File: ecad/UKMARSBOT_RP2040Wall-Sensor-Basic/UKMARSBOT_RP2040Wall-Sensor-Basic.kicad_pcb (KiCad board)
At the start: 2 copper layers, 80 x 31.2 mm, 32 parts, among them J1 Conn_01x16, T1 BC337-40, T2 BC337-40

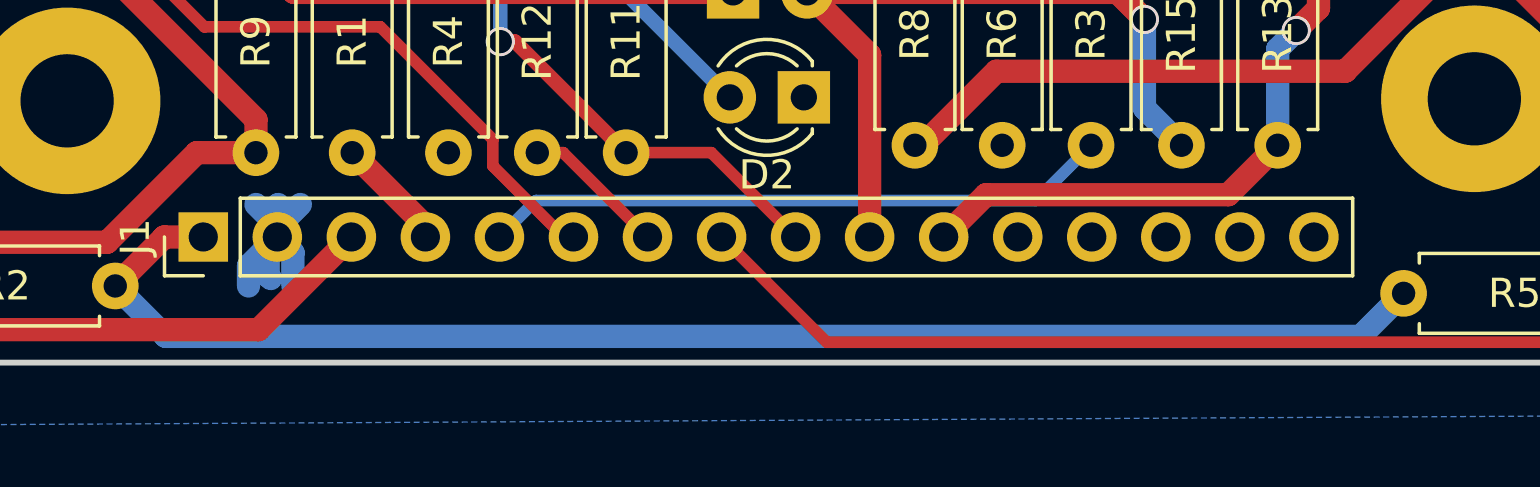
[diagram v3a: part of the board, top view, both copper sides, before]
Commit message: Updated silkscreen on wall sensor
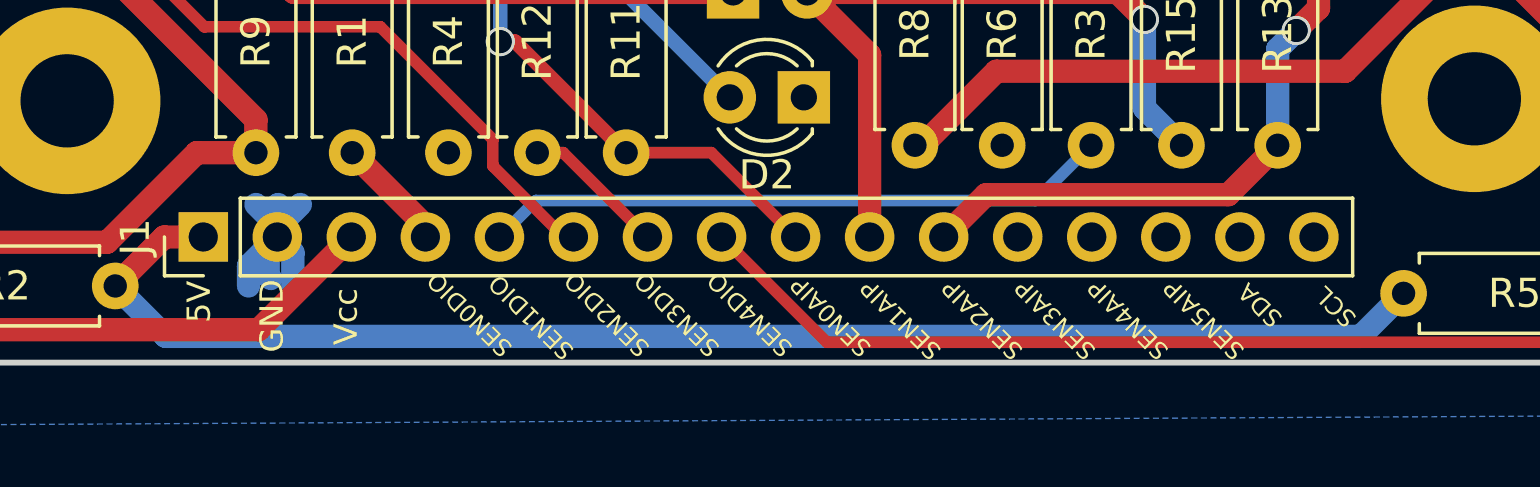
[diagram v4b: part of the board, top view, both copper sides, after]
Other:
- board text added: "5V"
- board text added: "GND"
- board text added: "SCL"
- board text added: "SDA"
- board text added: "SEN0AIP"
- board text added: "SEN0DIO"
- board text added: "SEN1AIP"
- board text added: "SEN1DIO"
- board text added: "SEN2AIP"
- board text added: "SEN2DIO"
- board text added: "SEN3AIP"
- board text added: "SEN3DIO"
- board text added: "SEN4AIP"
- board text added: "SEN4DIO"
- board text added: "SEN5AIP"
- board text added: "Vcc"
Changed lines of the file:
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@@
+		)
+	)
+	(gr_text "SEN2AIP"
+		(at 148.754 153.402 135)
+		(layer "F.SilkS")
+		(effects
+			(font
+				(size 0.6 0.6)
+				(thickness 0.15)
+			)
+			(justify left bottom)
+		)
+	)
+	(gr_text "SEN3AIP"
+		(at 151.254 153.402 135)
+		(layer "F.SilkS")
+		(effects
+			(font
+				(size 0.6 0.6)
+				(thickness 0.15)
+			)
+			(justify left bottom)
+		)
+	)
+	(gr_text "SEN1DIO"
+		(at 133.354 153.402 135)
+		(layer "F.SilkS")
+		(effects
+			(font
+				(size 0.6 0.6)
+				(thickness 0.15)
+			)
+			(justify left bottom)
+		)
+	)
+	(gr_text "SDA"
+		(at 157.658 152.286 135)
+		(layer "F.SilkS")
+		(effects
+			(font
+				(size 0.6 0.6)
+				(thickness 0.15)
+			)
+			(justify left bottom)
+		)
+	)
+	(gr_text "GND\n"
+		(at 123.368 153.556 90)
+		(layer "F.SilkS")
+		(effects
+			(font
+				(size 0.8 0.8)
+				(thickness 0.15)
+			)
+			(justify left bottom)
+		)
+	)
+	(gr_text "SEN0AIP"
+		(at 143.554 153.302 135)
+		(layer "F.SilkS")
+		(effects
+			(font
+				(size 0.6 0.6)
+				(thickness 0.15)
+			)
+			(justify left bottom)
+		)
+	)
+	(gr_text "SEN0DIO"
+		(at 131.242 153.302 135)
+		(layer "F.SilkS")
+		(effects
+			(font
+				(size 0.6 0.6)
+				(thickness 0.15)
+			)
+			(justify left bottom)
+		)
+	)
+	(gr_text "5V"
+		(at 120.868 152.54 90)
+		(layer "F.SilkS")
+		(effects
+			(font
+				(size 0.8 0.8)
+				(thickness 0.15)
+			)
+			(justify left bottom)
+		)
+	)
+	(gr_text "SEN5AIP"
+		(at 156.354 153.402 135)
+		(layer "F.SilkS")
+		(effects
+			(font
+				(size 0.6 0.6)
+				(thickness 0.15)
+			)
+			(justify left bottom)
+		)
+	)
+	(gr_text "SEN4AIP"
+		(at 153.754 153.402 135)
+		(layer "F.SilkS")
+		(effects
+			(font
+				(size 0.6 0.6)
+				(thickness 0.15)
+			)
+			(justify left bottom)
+		)
+	)
+	(gr_text "SCL"
+		(at 160.198 152.286 135)
+		(layer "F.SilkS")
+		(effects
+			(font
+				(size 0.6 0.6)
+				(thickness 0.15)
+			)
+			(justify left bottom)
+		)
+	)
+	(gr_text "SEN2DIO"
+		(at 135.954 153.302 135)
+		(layer "F.SilkS")
+		(effects
+			(font
+				(size 0.6 0.6)
+				(thickness 0.15)
+			)
+			(justify left bottom)
+		)
+	)
+	(gr_text "SEN3DIO"
+		(at 138.354 153.302 135)
+		(layer "F.SilkS")
+		(effects
+			(font
+				(size 0.6 0.6)
+				(thickness 0.15)
+			)
+			(justify left bottom)
+		)
+	)
+	(gr_text "Vcc"
+		(at 125.908 153.302 90)
+		(layer "F.SilkS")
+		(effects
+			(font
+				(size 0.8 0.8)
+				(thickness 0.15)
+			)
+			(justify left bottom)
+		)
+	)
+	(gr_text "SEN4DIO"
+		(at 140.854 153.302 135)
+		(layer "F.SilkS")
+		(effects
+			(font
+				(size 0.6 0.6)
+				(thickness 0.15)
+			)
+			(justify left bottom)
+		)
+	)
+	(gr_text "SEN1AIP"
+		(at 145.954 153.402 135)
+		(layer "F.SilkS")
+		(effects
+			(font
+				(size 0.6 0.6)
+				(thickness 0.15)
+			)
+			(justify left bottom)
 		)
 	)

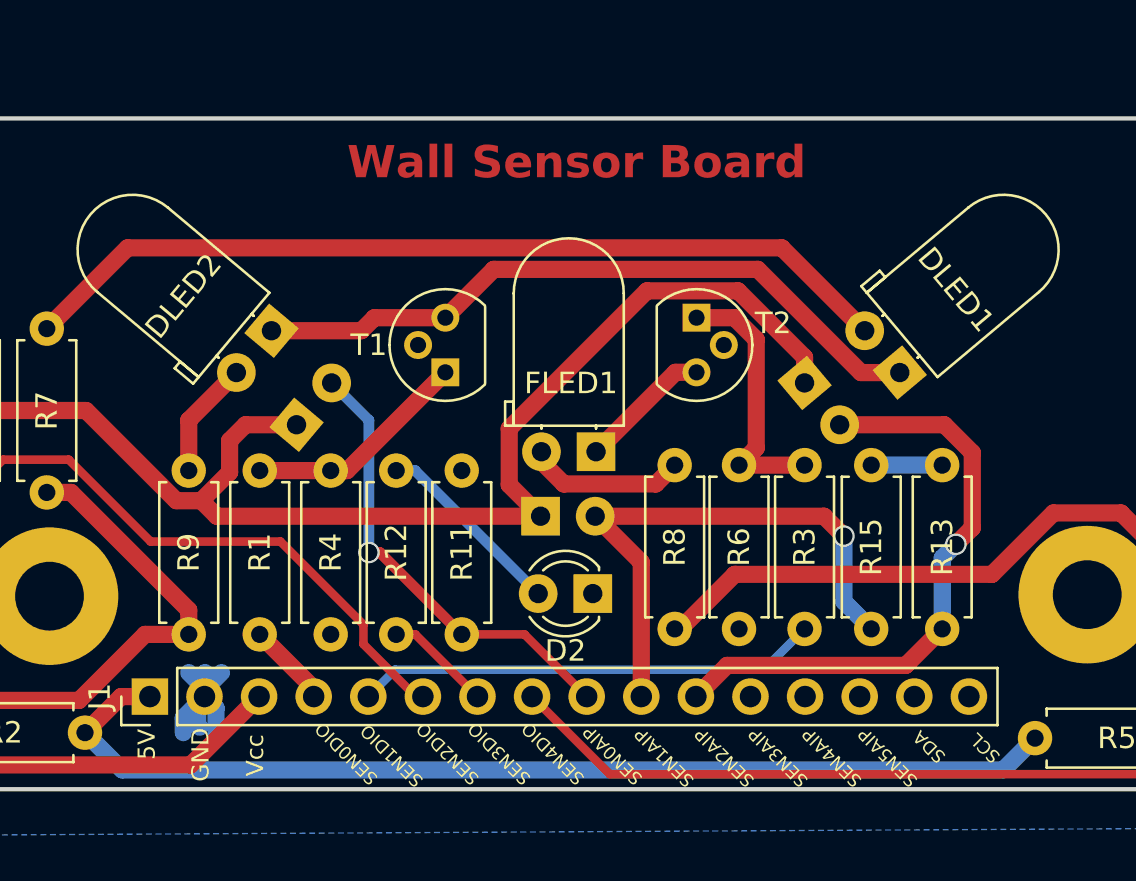
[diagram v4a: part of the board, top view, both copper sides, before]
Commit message: Updates to wall sensor based on feedback
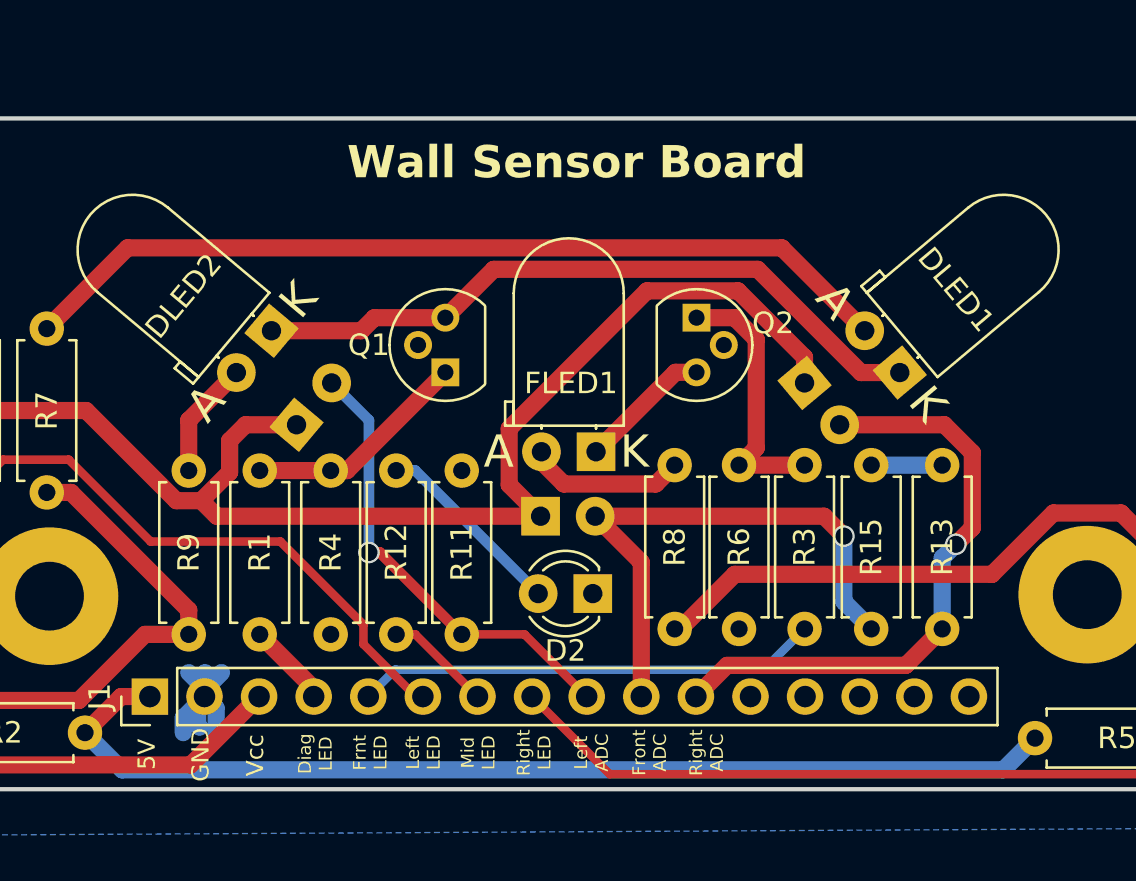
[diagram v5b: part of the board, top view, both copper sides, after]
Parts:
- renumbered T1 to Q1, T2 to Q2
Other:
- board text added: "A"
- board text added: "C"
- board text added: "Diag LED"
- board text added: "E"
- board text added: "Frnt LED"
- board text added: "Front ADC"
- board text added: "K"
- board text added: "Left ADC"
- board text added: "Left LED"
- board text added: "Mid LED"
- board text added: "Right ADC"
- board text added: "Right LED"
- board text removed: "SCL"
- board text removed: "SDA"
- board text removed: "SEN0AIP"
- board text removed: "SEN0DIO"
- board text removed: "SEN1AIP"
- board text removed: "SEN1DIO"
- board text removed: "SEN2AIP"
- board text removed: "SEN2DIO"
- board text removed: "SEN3AIP"
- board text removed: "SEN3DIO"
- board text removed: "SEN4AIP"
- board text removed: "SEN4DIO"
- board text removed: "SEN5AIP"
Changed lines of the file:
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@@
 	(net 16 "SEN0DI0")
 	(net 17 "SEN4DI0")
-	(net 18 "Net-(T1-B)")
-	(net 19 "Net-(T2-B)")
+	(net 18 "Net-(Q1-B)")
+	(net 19 "Net-(Q2-B)")
 	(net 20 "Net-(C1-Pad1)")
 	(net 21 "Net-(C2-Pad1)")
@@
 		(descr "TO-92 leads molded, narrow, drill 0.75mm (see NXP sot054_po.pdf)")
 		(tags "to-92 sc-43 sc-43a sot54 PA33 transistor")
-		(property "Reference" "T1"
+		(property "Reference" "Q1"
 			(at 1.27 -3.56 180)
 			(layer "F.SilkS")
@@
 			)
 			(remove_unused_layers no)
-			(net 18 "Net-(T1-B)")
+			(net 18 "Net-(Q1-B)")
 			(pinfunction "B")
 			(pintype "input")
@@
 		(descr "TO-92 leads molded, narrow, drill 0.75mm (see NXP sot054_po.pdf)")
 		(tags "to-92 sc-43 sc-43a sot54 PA33 transistor")
-		(property "Reference" "T2"
+		(property "Reference" "Q2"
 			(at 0.254 -3.56 180)
 			(layer "F.SilkS")
@@
 			)
 			(remove_unused_layers no)
-			(net 19 "Net-(T2-B)")
+			(net 19 "Net-(Q2-B)")
 			(pinfunction "B")
 			(pintype "input")
@@
 	)
 	(footprint "LED_THT:LED_D5.0mm_Horizontal_O1.27mm_Z3.0mm"
-		(locked yes)
 		(layer "F.Cu")
 		(at 126.2019 132.5716 -130)
@@
 			)
 			(remove_unused_layers no)
-			(net 19 "Net-(T2-B)")
+			(net 19 "Net-(Q2-B)")
 			(pintype "passive")
 		)
@@
 			)
 			(remove_unused_layers no)
-			(net 18 "Net-(T1-B)")
+			(net 18 "Net-(Q1-B)")
 			(pintype "passive")
 		)
@@
 			)
 			(remove_unused_layers no)
-			(net 18 "Net-(T1-B)")
+			(net 18 "Net-(Q1-B)")
 			(pintype "passive")
 		)
@@
 			)
 			(remove_unused_layers no)
-			(net 19 "Net-(T2-B)")
+			(net 19 "Net-(Q2-B)")
 			(pintype "passive")
 		)
@@
 	)
 	(footprint "LED_THT:LED_D5.0mm_Horizontal_O1.27mm_Z3.0mm"
-		(locked yes)
 		(layer "B.Cu")
 		(at 127.3673 136.9458 50)
@@
 		(layer "User.2")
 	)
-	(gr_text "Wall Sensor Board"
-		(at 129.718 125.616 0)
-		(layer "F.Cu")
+	(gr_text "E"
+		(at 125.908 137.3 50)
+		(layer "B.SilkS")
 		(effects
 			(font
-				(size 1.5 1.5)
-				(thickness 0.3)
-				(bold yes)
+				(size 1 1)
+				(thickness 0.1875)
 			)
-			(justify left bottom)
+			(justify left bottom mirror)
+		)
+	)
+	(gr_text "C\n"
+		(at 130.734 133.744 50)
+		(layer "B.SilkS")
+		(effects
+			(font
+				(size 1 1)
+				(thickness 0.1875)
+			)
+			(justify left bottom mirror)
 		)
 	)
@@
 		)
 	)
+	(gr_text "C\n"
+		(at 143.434 141.618 0)
+		(layer "B.SilkS")
+		(effects
+			(font
+				(size 1 1)
+				(thickness 0.1875)
+			)
+			(justify left bottom mirror)
+		)
+	)
 	(gr_text "${designer}"
 		(at 170.612 130.95 315)
@@
 		)
 	)
-	(gr_text "SEN2AIP"
-		(at 148.754 153.402 135)
+	(gr_text "E"
+		(at 149.784 135.014 310)
+		(layer "B.SilkS")
+		(effects
+			(font
+				(size 1 1)
+				(thickness 0.1875)
+			)
+			(justify left bottom mirror)
+		)
+	)
+	(gr_text "C\n"
+		(at 152.578 139.332 310)
+		(layer "B.SilkS")
+		(effects
+			(font
+				(size 1 1)
+				(thickness 0.1875)
+			)
+			(justify left bottom mirror)
+		)
+	)
+	(gr_text "E"
+		(at 137.592 141.618 0)
+		(layer "B.SilkS")
+		(effects
+			(font
+				(size 1 1)
+				(thickness 0.1875)
+			)
+			(justify left bottom mirror)
+		)
+	)
+	(gr_text "Right\nADC"
+		(at 147.275 152.2 90)
 		(layer "F.SilkS")
 		(effects
@@
 				(thickness 0.15)
 			)
+			(justify bottom)
+		)
+	)
+	(gr_text "K"
+		(at 127.686 132.22 50)
+		(layer "F.SilkS")
+		(effects
+			(font
+				(size 1.5 1.5)
+				(thickness 0.1875)
+			)
 			(justify left bottom)
 		)
 	)
-	(gr_text "SEN3AIP"
-		(at 151.254 153.402 135)
+	(gr_text "A"
+		(at 151.308 131.204 310)
 		(layer "F.SilkS")
 		(effects
 			(font
-				(size 0.6 0.6)
-				(thickness 0.15)
+				(size 1.5 1.5)
+				(thickness 0.1875)
 			)
 			(justify left bottom)
 		)
 	)
-	(gr_text "SEN1DIO"
-		(at 133.354 153.402 135)
+	(gr_text "Frnt\nLED"
+		(at 131.625 152.2 90)
 		(layer "F.SilkS")
 		(effects
@@
 				(thickness 0.15)
 			)
+			(justify bottom)
+		)
+	)
+	(gr_text "A"
+		(at 123.368 137.046 50)
+		(layer "F.SilkS")
+		(effects
+			(font
+				(size 1.5 1.5)
+				(thickness 0.1875)
+			)
 			(justify left bottom)
 		)
 	)
-	(gr_text "SDA"
-		(at 157.658 152.286 135)
+	(gr_text "Wall Sensor Board"
+		(at 129.718 125.616 0)
 		(layer "F.SilkS")
 		(effects
 			(font
-				(size 0.6 0.6)
-				(thickness 0.15)
+				(size 1.5 1.5)
+				(thickness 0.3)
+				(bold yes)
 			)
 			(justify left bottom)
@@
 		)
 	)
-	(gr_text "SEN0AIP"
-		(at 143.554 153.302 135)
+	(gr_text "Left\nADC"
+		(at 141.925 152.2 90)
 		(layer "F.SilkS")
 		(effects
@@
 				(thickness 0.15)
 			)
-			(justify left bottom)
+			(justify bottom)
 		)
 	)
-	(gr_text "SEN0DIO"
-		(at 131.242 153.302 135)
+	(gr_text "Diag\nLED"
+		(at 129.075 152.25 90)
 		(layer "F.SilkS")
 		(effects
@@
 				(thickness 0.15)
 			)
-			(justify left bottom)
+			(justify bottom)
 		)
 	)
 	(gr_text "5V"
-		(at 120.868 152.54 90)
+		(at 120.868 153 90)
 		(layer "F.SilkS")
 		(effects
@@
 		)
 	)
-	(gr_text "SEN5AIP"
-		(at 156.354 153.402 135)
+	(gr_text "A"
+		(at 136.068 139.078 0)
 		(layer "F.SilkS")
 		(effects
 			(font
-				(size 0.6 0.6)
-				(thickness 0.15)
+				(size 1.5 1.5)
+				(thickness 0.1875)
 			)
 			(justify left bottom)
 		)
 	)
-	(gr_text "SEN4AIP"
-		(at 153.754 153.402 135)
+	(gr_text "K"
+		(at 155.626 136.03 310)
 		(layer "F.SilkS")
 		(effects
 			(font
-				(size 0.6 0.6)
-				(thickness 0.15)
+				(size 1.5 1.5)
+				(thickness 0.1875)
 			)
 			(justify left bottom)
 		)
 	)
-	(gr_text "SCL"
-		(at 160.198 152.286 135)
+	(gr_text "Left\nLED"
+		(at 134.1 152.2 90)
 		(layer "F.SilkS")
 		(effects
@@
 				(thickness 0.15)
 			)
-			(justify left bottom)
+			(justify bottom)
 		)
 	)
-	(gr_text "SEN2DIO"
-		(at 135.954 153.302 135)
+	(gr_text "Mid\nLED"
+		(at 136.65 152.2 90)
 		(layer "F.SilkS")
 		(effects
@@
 				(thickness 0.15)
 			)
-			(justify left bottom)
+			(justify bottom)
 		)
 	)
-	(gr_text "SEN3DIO"
-		(at 138.354 153.302 135)
+	(gr_text "Vcc"
+		(at 125.908 153.302 90)
 		(layer "F.SilkS")
 		(effects
 			(font
-				(size 0.6 0.6)
+				(size 0.8 0.8)
 				(thickness 0.15)
 			)
@@
 		)
 	)
-	(gr_text "Vcc"
-		(at 125.908 153.302 90)
+	(gr_text "Right\nLED"
+		(at 139.25 152.2 90)
 		(layer "F.SilkS")
 		(effects
 			(font
-				(size 0.8 0.8)
+				(size 0.6 0.6)
 				(thickness 0.15)
 			)
-			(justify left bottom)
+			(justify bottom)
 		)
 	)
-	(gr_text "SEN4DIO"
-		(at 140.854 153.302 135)
+	(gr_text "K"
+		(at 142.418 139.078 0)
 		(layer "F.SilkS")
 		(effects
 			(font
-				(size 0.6 0.6)
-				(thickness 0.15)
+				(size 1.5 1.5)
+				(thickness 0.1875)
 			)
 			(justify left bottom)
 		)
 	)
-	(gr_text "SEN1AIP"
-		(at 145.954 153.402 135)
+	(gr_text "Front\nADC"
+		(at 144.625 152.2 90)
 		(layer "F.SilkS")
 		(effects
@@
 				(thickness 0.15)
 			)
-			(justify left bottom)
+			(justify bottom)
 		)
 	)
@@
 		(members "0e0d40c5-8c10-45a9-986b-fb2de8d5d8ab" "2266d8cc-a5b9-496f-a2b3-43ded6c794fe")
 	)
-	(group ""
-		(locked yes)
-		(members "49b3aba5-9199-4264-8abf-1bcb7c81eaec" "4f064650-dfcb-44de-b835-755be681dc67")
-	)
 )
